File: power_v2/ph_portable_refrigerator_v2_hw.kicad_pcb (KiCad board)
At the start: 2 copper layers, 45 x 188.1 mm, 193 parts, among them IC1 SC16IS750IBS,128, J1 SIM7100-6-1-15-00-A_REVC, J1 microSD_Card, J10 Extra, J11 refrigerator, J12 Conn_01x04, J13 Extra, J14 Conn_01x03_Pin, J15 USB_C_Receptacle_USB2.0, J2 Conn_01x06_Pin, J3 Conn_01x06_Pin, J5 lamp, J6 lock_latch, J7 Conn_02x08_Odd_Even, J8 Header_4P_2.54mm, J9 sensor, Q1 C1815, Q10 S8050, Q11 S8050, Q12 C1815_SOT23, Q13 C1815_SOT23, Q14 C1815_SOT23, Q2 C1815_SOT23, Q3 C1815, Q4 AO3400A, Q5 C1815, Q6 AO3400A, Q7 C1815_SOT23, Q8 C1815, Q9 2SC1815-HF, U1 ESP32-WROOM, U10 MAX485, U11 CP2102-GM, U2 TPS5430DDAR, U3 AMS1117-3.3, U4 DS1307Z+_SMD, U5 MIC29302WU, U6 MAX31865_TQFN, U7 NEO-M8M, U8 SIM_COM_A7670, Y1 32.768, Y2 14.7456 MHz

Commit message: Oder PCB, Viet tai lieu mo ta hardware
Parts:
- removed the C1 at (38.5, 198.1)
- removed the J1 at (57.5, 203.2)
- removed J2: Conn_01x06_Pin, Connector_PinHeader_1.27mm:PinHeader_1x06_P1.27mm_Horizontal
- renumbered AE1 to AT1, AE2 to AT2
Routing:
- net (no net): track 75.6 -> 0.00 mm
- net /I2C Expand Block/Vin: track 127.2 -> 100.6 mm
- net /I2C Expand Block/P4: track 42.2 -> 41.5 mm
- net GND: track 726.9 -> 727.4 mm, vias 357 -> 364
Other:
- board size 45 x 188.1 mm -> 45 x 172 mm
- board text added: "AI0"
- board text added: "CLK"
- board text added: "Connect board Display"
- board text added: "DATA"
- board text added: "DET"
- board text added: "IO34"
- board text added: "IQR"
- board text added: "LCD_BL"
- board text added: "LCD_CS"
- board text added: "LCD_DC"
- board text added: "LCD_RST"
- board text added: "MOSI"
- board text added: "RST"
- board text added: "SCL"
- board text added: "SD CARD"
- board text added: "SDA"
- board text added: "SPI_CLK"
- board text added: "Version: 2 Maker: P.D.H Date: 05_2023"
- board text added: "vsim"
- board text added: "x"

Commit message: Han Board MCU va board Display
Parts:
- C41, C43: value 100nF -> 10uF
- renumbered AT1 to AE1, AT2 to AE2
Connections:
- C41 pad 1: +3.3V -> +3V3
- C42 pad 1: +3.3V -> +3V3
- U11 pad 6: +3.3V -> +3V3
- U11 pad 7: +3.3V -> +3V3
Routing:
- net +3V3: track 436.6 -> 441.3 mm
- net +3.3V: track 4.66 -> 0.00 mm

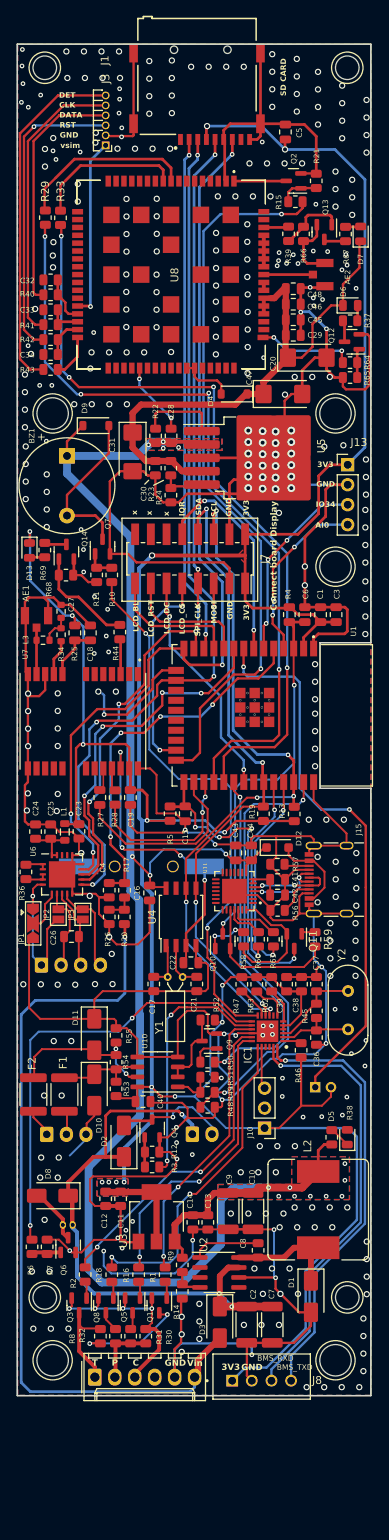
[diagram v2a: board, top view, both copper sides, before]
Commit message: Modify tx/rx UART0, LED GPS, pin rst/clk sim card
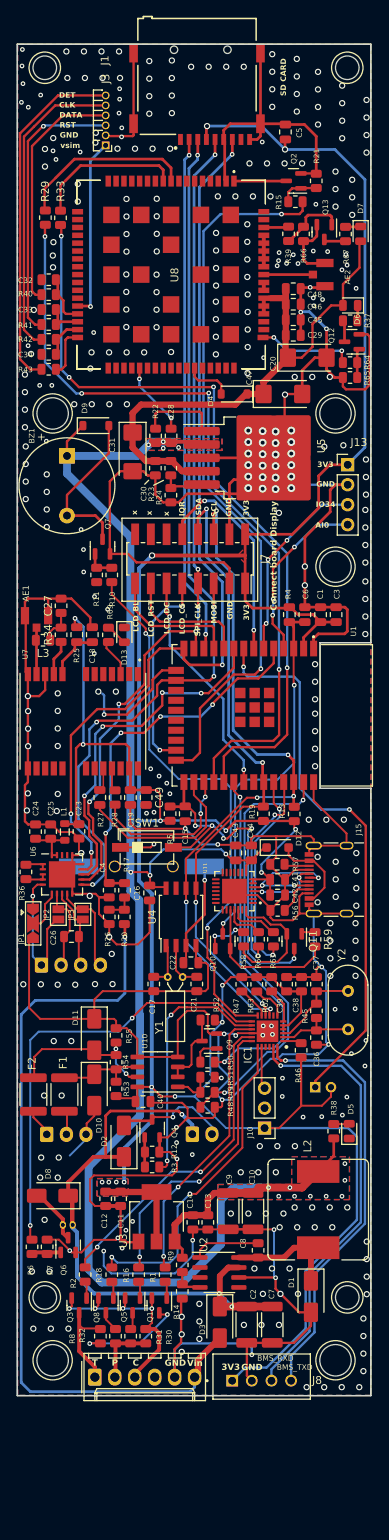
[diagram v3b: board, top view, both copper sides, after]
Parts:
- removed Q14: C1815_SOT23, Package_TO_SOT_SMD:SOT-23
- removed R44, R68: 4.7K, Resistor_SMD:R_0805_2012Metric
- added C49: 100nF, Capacitor_SMD:C_0805_2012Metric, F.Cu at (51.4, 117.9)
- added SW1: button_2pin, Button_Switch_SMD:SW_DIP_SPSTx01_Slide_6.7x4.1mm_W6.73mm_P2.54mm_LowProfile_JPin, F.Cu at (51.5, 124.2)
- C18: value 100nF -> 10uF
- C19: value 100nF -> 1uF
- C27, L3, R34: footprint Resistor_SMD:R_0603_1608Metric -> Resistor_SMD:R_0805_2012Metric
- Q10, Q11: value S8050 -> C1815
- R23: value 5.1k/1% -> 240R/1%
- R24: value 10.5k/1% -> 120R/1%
- R65, R66: value 4.7K -> 47K
- moved D13 16.2 mm to (48.6, 97.2)
- moved R69 13.5 mm to (46.6, 97.2), turned to 90 degrees
- moved D5 0.81 mm to (77.2, 160.3)
- moved R38 0.81 mm to (75.3, 160.3)
- moved C27 0.71 mm to (40.6, 93.5)
- moved C18 0.34 mm to (44.5, 97.2)
- moved R25 0.34 mm to (42.6, 97.2)
- moved R41 0.24 mm to (39.0, 57.7)
- moved C32 0.24 mm to (39.0, 52.0)
- moved C33 0.24 mm to (39.0, 55.8)
- moved C34 0.24 mm to (39.0, 61.5)
- moved R40 0.24 mm to (39.0, 53.9)
- moved R42 0.24 mm to (39.0, 59.6)
- moved R43 0.24 mm to (39.0, 63.4)
- turned D6 to 180 degrees
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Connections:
- D13 pad 1: +3V3 -> Net-(D13-A)
- D13 pad 2: Net-(D13-K) -> GND
- J3 pad 3: /GSM Block/sim_rst# -> /GSM Block/sim_clk#
- J3 pad 5: /GSM Block/sim_clk# -> /GSM Block/sim_rst#
- R69 pad 1: Net-(Q14-C) -> /GPS/Timepluse
- R69 pad 2: Net-(D13-K) -> Net-(D13-A)
- U1 pad 34: /ESP_TX -> /ESP_RX
- U1 pad 35: /ESP_RX -> /ESP_TX
- U1 pad 39_1: (no net) -> GND
- U1 pad 39_2: (no net) -> GND
- U1 pad 39_3: (no net) -> GND
- U1 pad 39_4: (no net) -> GND
- U1 pad 39_5: (no net) -> GND
- U1 pad 39_6: (no net) -> GND
- U1 pad 39_7: (no net) -> GND
- U1 pad 39_8: (no net) -> GND
- U1 pad 39_9: (no net) -> GND
- U7 pad 22: +BATT -> unconnected-(U7-V_BCKP-Pad22)
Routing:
- net +BATT: track 39.2 -> 14.9 mm, vias 4 -> 1
- net Net-(Q14-B): track 13.5 -> 0.00 mm
- net GND: track 727.4 -> 714.6 mm, vias 364 -> 369
- net +3V3: track 441.3 -> 434.4 mm, vias 17 -> 18
- net ESP_IO0: track 40.2 -> 46.5 mm, vias 4 -> 5
- net /MCU Block/USB_D-: track 10.8 -> 16.7 mm, vias 2 -> 3
- net Net-(Q14-C): track 2.83 -> 0.00 mm
- net Net-(D13-A): track 0.00 -> 2.79 mm
- net Net-(D13-K): track 1.98 -> 0.00 mm
- net Net-(C27-Pad1): track 3.93 -> 5.87 mm
- net /AI01: track 47.4 -> 49.3 mm
- net /GPS_TXD: track 24.4 -> 22.5 mm
- net /GPS_RXD: track 21.4 -> 19.9 mm
- net +5V: track 236.0 -> 237.3 mm
- net /ESP_TX: track 24.9 -> 26.0 mm
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
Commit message: update
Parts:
- removed G***: LOGO, 01phkicad:logo
